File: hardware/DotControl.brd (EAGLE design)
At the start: 30.7 x 65 mm, 45 parts, among them CN1 1X4-BIG, IC1 MCP1703CB, J3 USB-MICROB, SW2 Previous, SW5 Previous, SW6 Next, SW8 Ok, U1 ATMEGA328P-MU-QFN32, U2 TMP102, U3 ATSHA204-TSU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

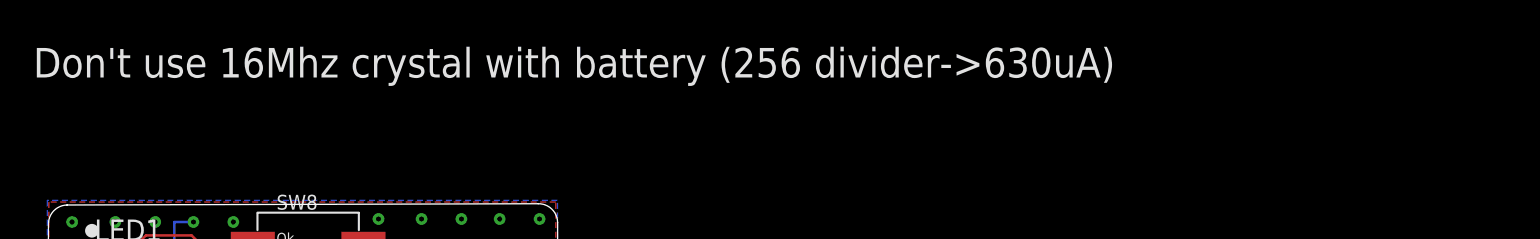
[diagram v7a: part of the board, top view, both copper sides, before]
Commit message: Update LeLe: 16Mhz with 256 divider = 5uA draw
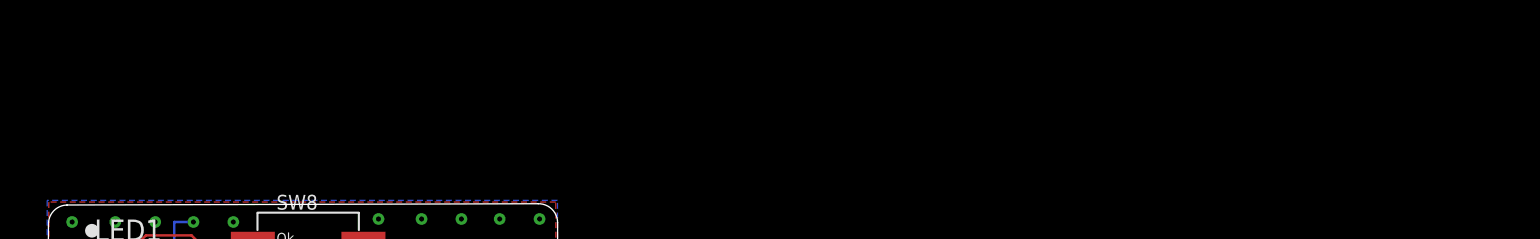
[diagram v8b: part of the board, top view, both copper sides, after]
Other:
- board text removed: "Don't use 16Mhz crystal with battery (256 divider->630uA)"
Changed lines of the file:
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@@
 <text x="9.4234" y="7.8486" size="0.8128" layer="21" rot="R90">SDA</text>
 <text x="20.5486" y="10.16" size="0.8128" layer="21" rot="R270">GND</text>
-<text x="-0.8382" y="72.5932" size="1.778" layer="21">Don't use 16Mhz crystal with battery (256 divider-&gt;630uA)</text>
 <wire x1="26.289" y1="42.5958" x2="26.289" y2="43.0784" width="0.1524" layer="22"/>
 <wire x1="26.289" y1="43.0784" x2="26.289" y2="43.5356" width="0.1524" layer="22"/>
